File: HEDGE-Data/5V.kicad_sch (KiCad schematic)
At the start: 11 parts, among them U2 MAX20402AFLA/VY+

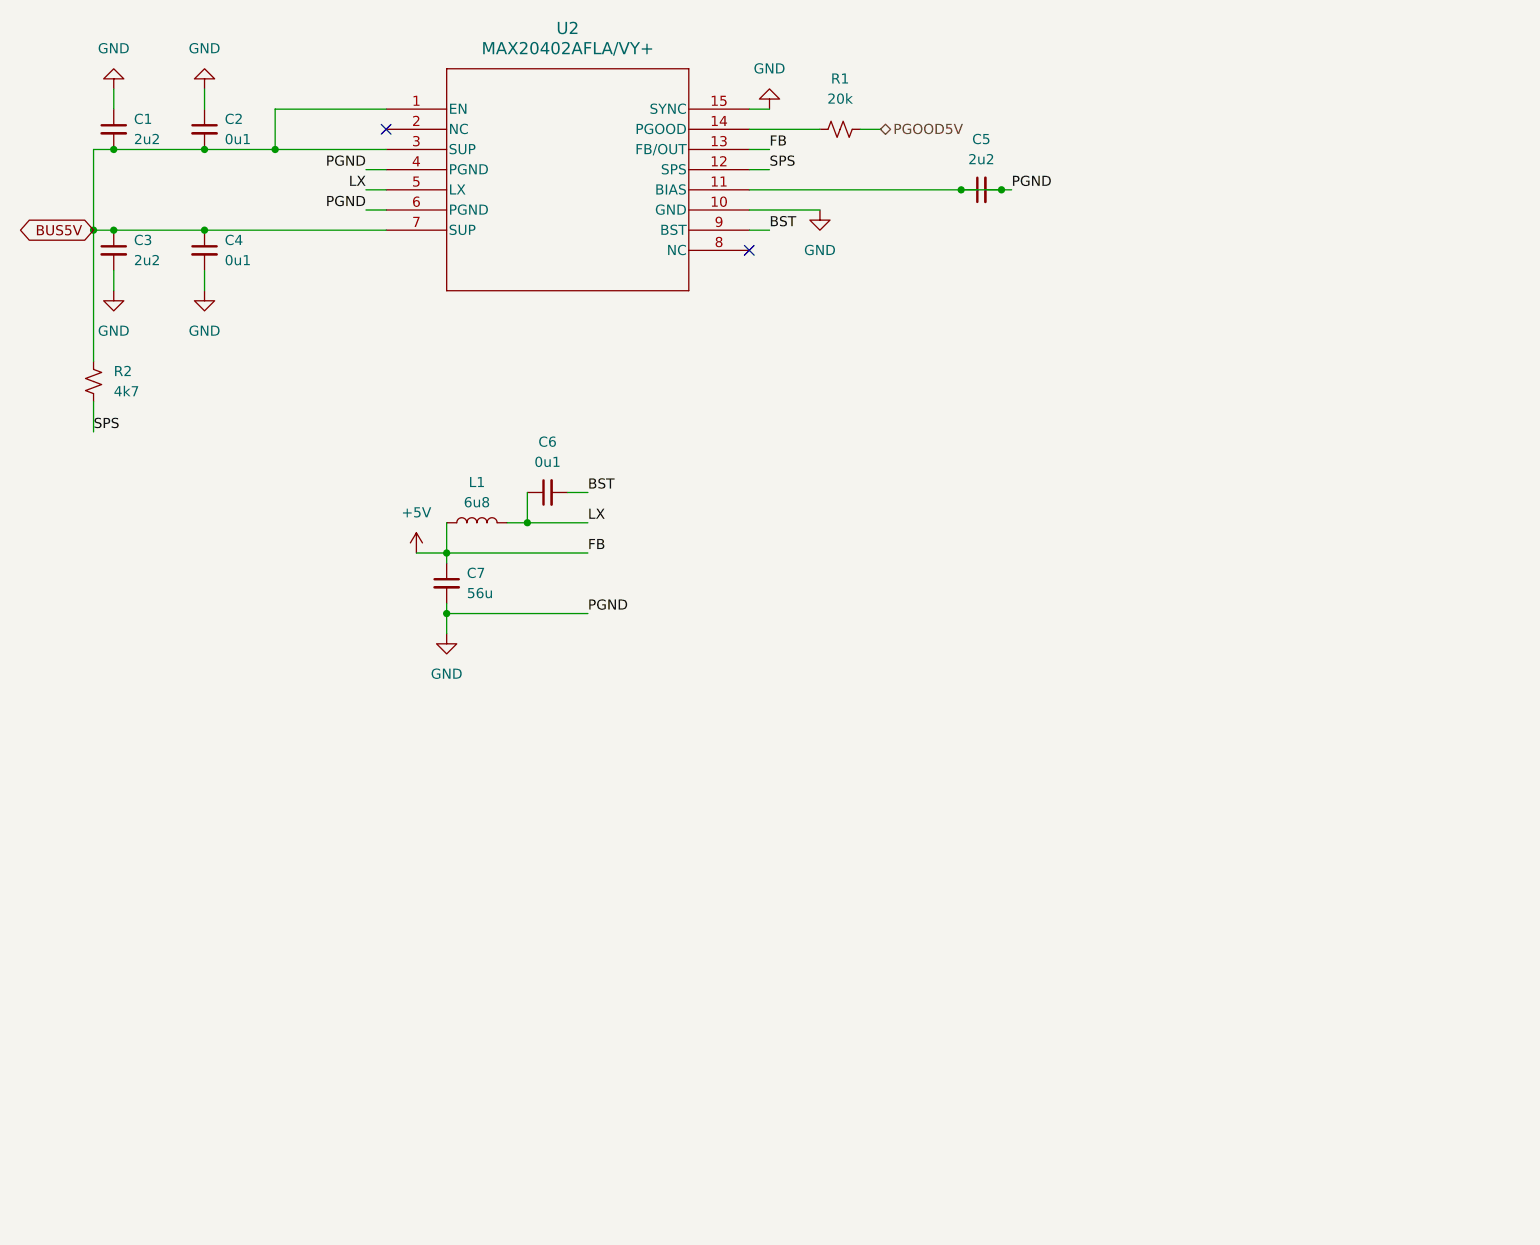
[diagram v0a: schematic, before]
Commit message: Repair KiCAD files; modularize common circuits
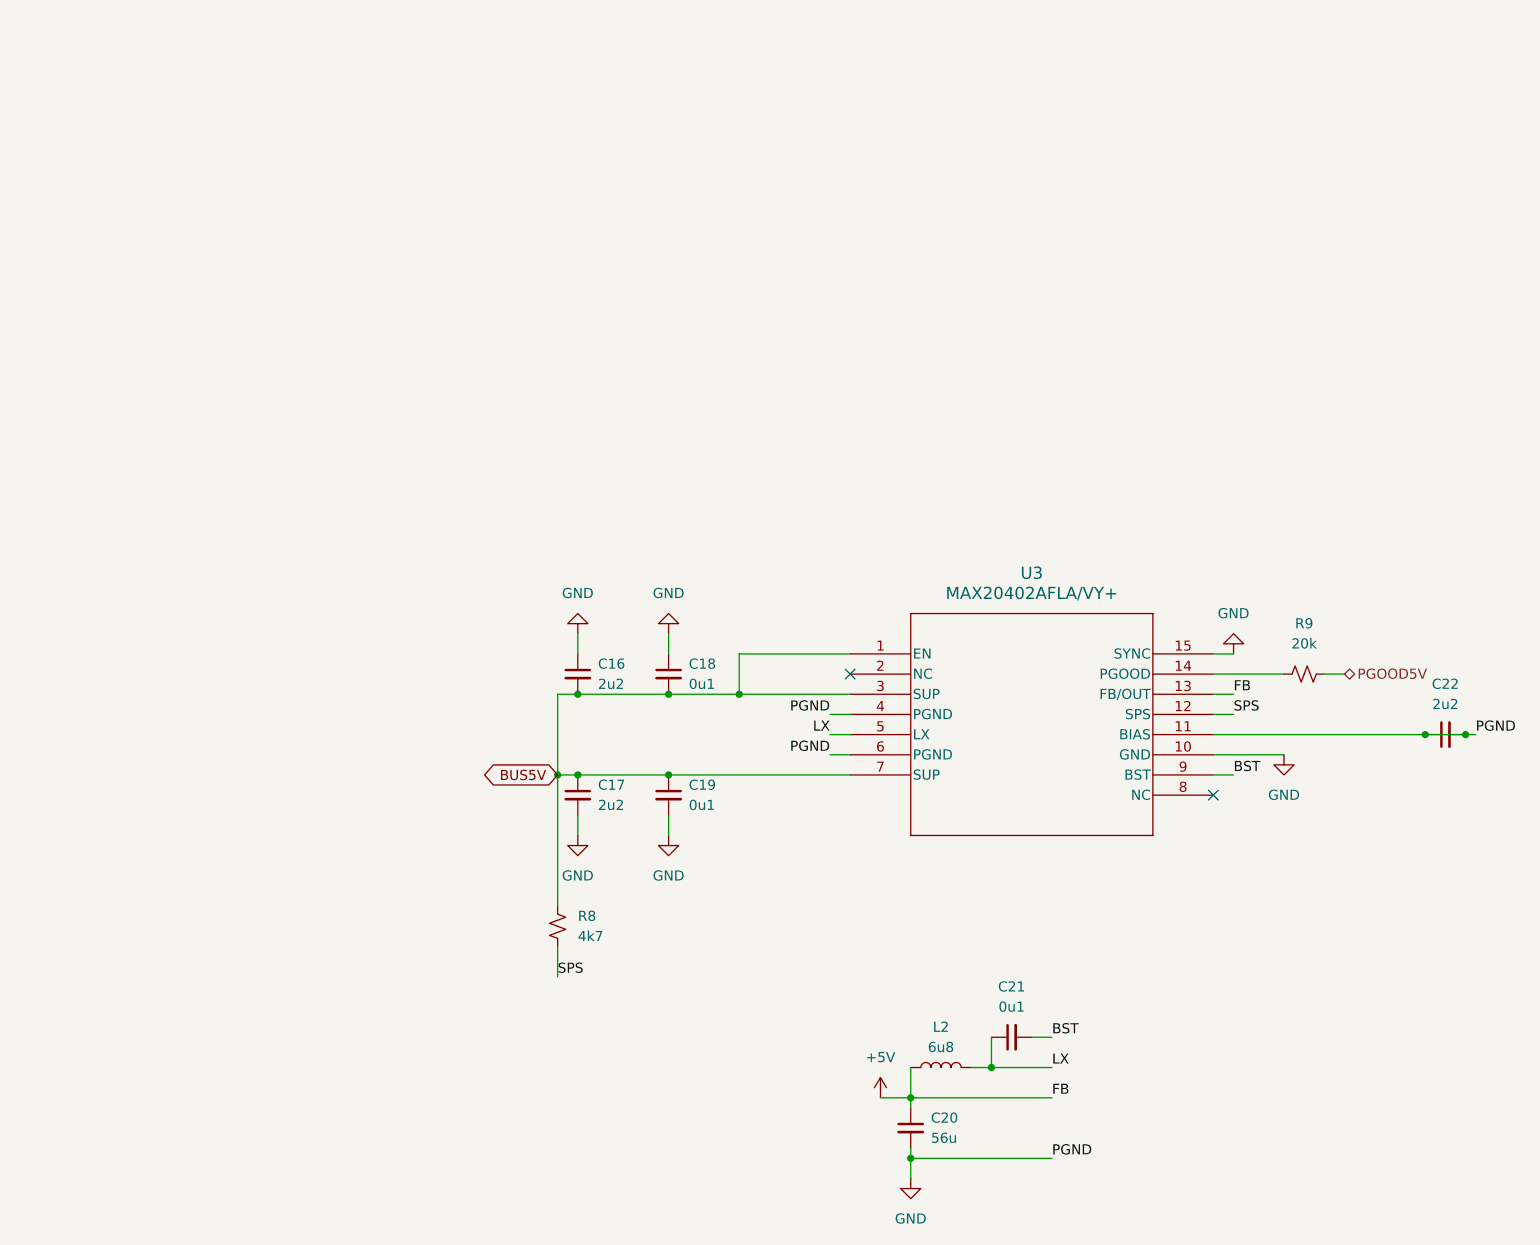
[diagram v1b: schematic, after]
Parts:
- removed C1, C3, C5: 2u2, symbol Device:C_Small
- removed C2, C4, C6: 0u1, symbol Device:C_Small
- removed C7: 56u, symbol Device:C_Small
- removed L1: 6u8, symbol Device:L
- removed R1: 20k, symbol Device:R_Small_US
- removed R2: 4k7, symbol Device:R_Small_US
- removed U2: MAX20402AFLA/VY+, 21-100532_90-100188_ADI, symbol MAX20402A:MAX20402AFLA_VY+
- added C16, C17, C22: 2u2, symbol Device:C_Small
- added C18, C19, C21: 0u1, symbol Device:C_Small
- added C20: 56u, symbol Device:C_Small
- added L2: 6u8, symbol Device:L
- added R8: 4k7, symbol Device:R_Small_US
- added R9: 20k, symbol Device:R_Small_US
- added U3: MAX20402AFLA/VY+, 21-100532_90-100188_ADI, symbol MAX20402A:MAX20402AFLA_VY+
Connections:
- net +5V: now also C20.1, L2.1, U3.13 (FB/OUT)
- net BST: now also C21.2, U3.9 (BST)
- net BUS5V: now also C16.2, C17.1, C18.2, C19.1, R8.2, U3.1 (EN), U3.3 (SUP), U3.7 (SUP)
- net GND: now also C16.1, C17.2, C18.1, C19.2, C20.2, C22.1, C22.2, U3.10 (GND), U3.11 (BIAS), U3.15 (SYNC), U3.4 (PGND), U3.6 (PGND)
- net LX: now also C21.1, L2.2, U3.5 (LX)
- net PGOOD5V: now also R9.2
- net SPS: now also R8.1, U3.12 (SPS)
- new net: R9.1, U3.14 (PGOOD)
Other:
- company: (none) -> Spacecraft Design Lab
- title: (none) -> HEDGE-Data PCB

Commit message: Refactor Data PCB files; enter RS485; enter Iridium radio power
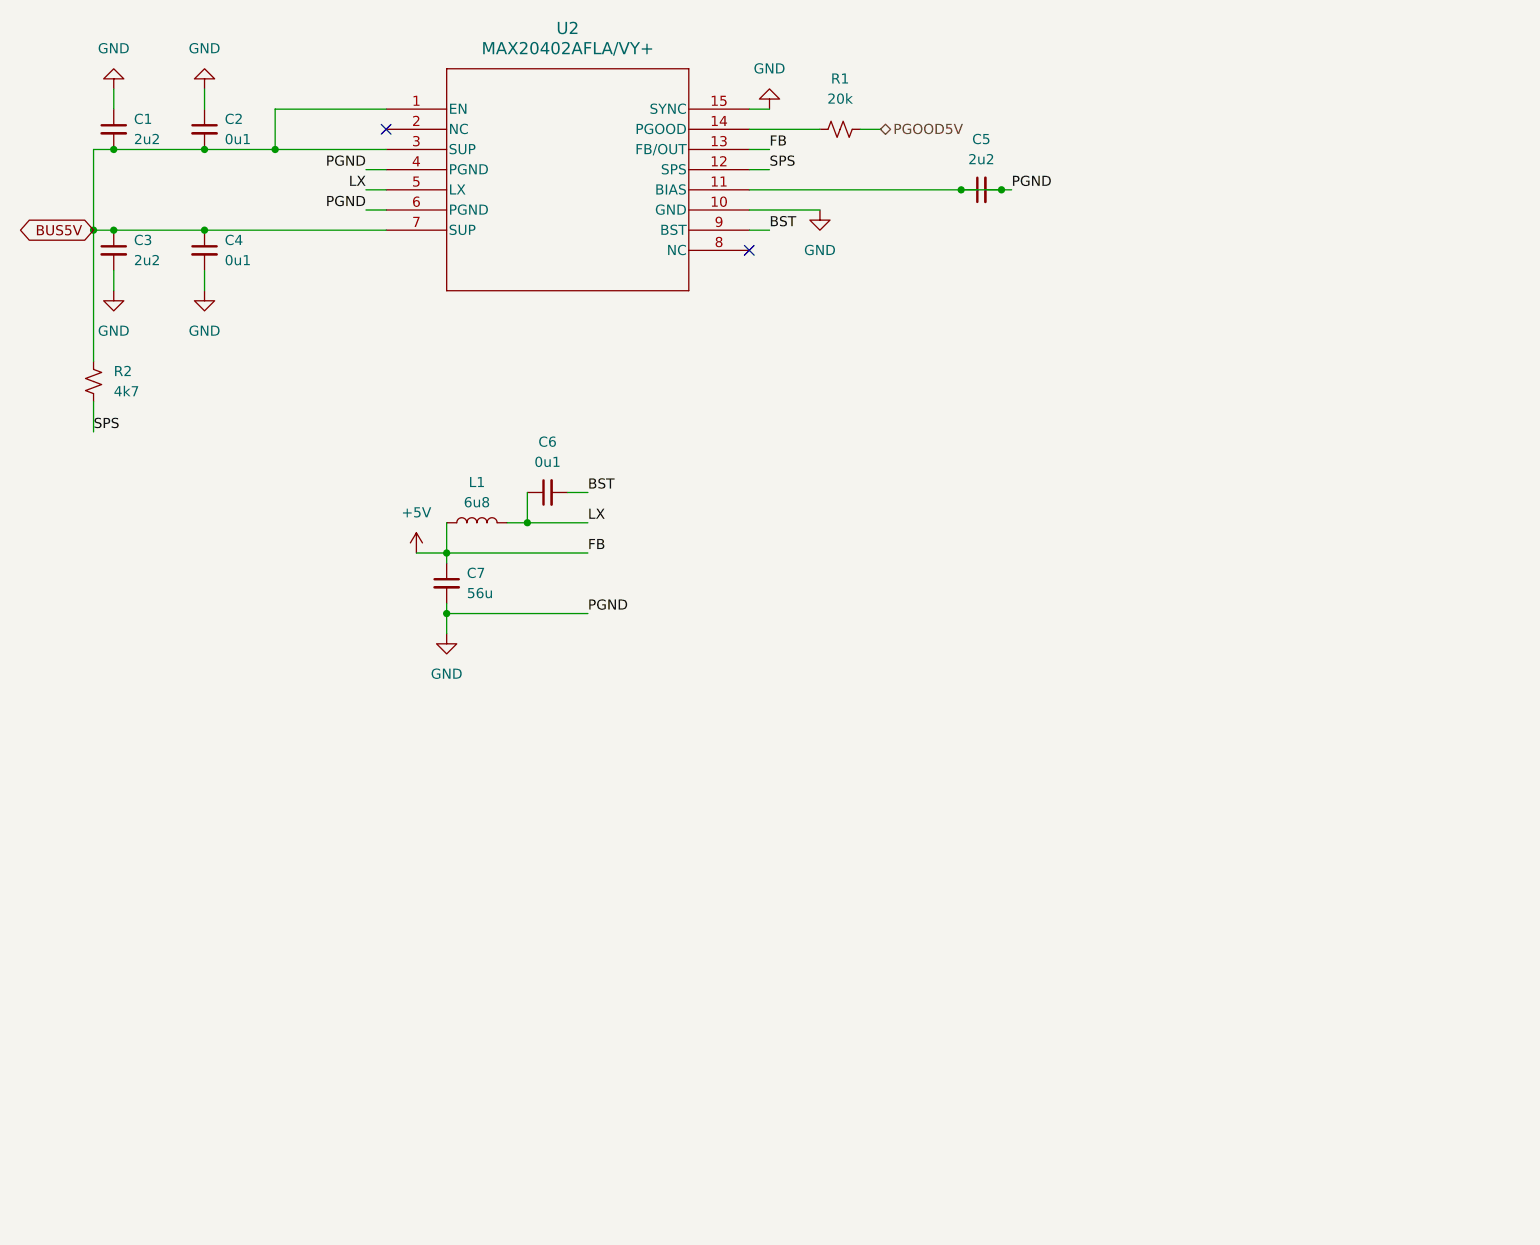
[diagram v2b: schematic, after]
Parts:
- removed C16, C17, C22: 2u2, symbol Device:C_Small
- removed C18, C19, C21: 0u1, symbol Device:C_Small
- removed C20: 56u, symbol Device:C_Small
- removed L2: 6u8, symbol Device:L
- removed R8: 4k7, symbol Device:R_Small_US
- removed R9: 20k, symbol Device:R_Small_US
- removed U3: MAX20402AFLA/VY+, 21-100532_90-100188_ADI, symbol MAX20402A:MAX20402AFLA_VY+
- added C1, C3, C5: 2u2, symbol Device:C_Small
- added C2, C4, C6: 0u1, symbol Device:C_Small
- added C7: 56u, symbol Device:C_Small
- added L1: 6u8, symbol Device:L
- added R1: 20k, symbol Device:R_Small_US
- added R2: 4k7, symbol Device:R_Small_US
- added U2: MAX20402AFLA/VY+, 21-100532_90-100188_ADI, symbol MAX20402A:MAX20402AFLA_VY+
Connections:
- net +5V: now also C7.1, L1.1, U2.13 (FB/OUT)
- net BST: now also C6.2, U2.9 (BST)
- net BUS5V: now also C1.2, C2.2, C3.1, C4.1, R2.2, U2.1 (EN), U2.3 (SUP), U2.7 (SUP)
- net GND: now also C1.1, C2.1, C3.2, C4.2, C5.1, C5.2, C7.2, U2.10 (GND), U2.11 (BIAS), U2.15 (SYNC), U2.4 (PGND), U2.6 (PGND)
- net LX: now also C6.1, L1.2, U2.5 (LX)
- net PGOOD5V: now also R1.2
- net SPS: now also R2.1, U2.12 (SPS)
- new net: R1.1, U2.14 (PGOOD)
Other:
- company: Spacecraft Design Lab -> (none)
- title: HEDGE-Data PCB -> (none)
